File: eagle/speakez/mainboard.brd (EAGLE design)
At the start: 22 parts, among them U1 +12v

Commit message: disconnected battery from V3v3
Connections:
- net N$16: no longer U$1.7
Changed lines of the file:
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@@
 <contactref element="U$1" pad="30"/>
 <contactref element="U$1" pad="3"/>
-<contactref element="U$1" pad="7"/>
 <wire x1="-32.01" y1="-79.73" x2="-46.62" y2="-81.28" width="0" layer="19" extent="1-1"/>
 <wire x1="-17.5768" y1="-20.955" x2="-32.01" y2="-79.73" width="0" layer="19" extent="1-1"/>
 <wire x1="-14.605" y1="-11.4808" x2="-17.5768" y2="-20.955" width="0" layer="19" extent="1-1"/>
-<wire x1="-26.035" y1="-14.478" x2="-17.5768" y2="-20.955" width="0" layer="19" extent="1-1"/>
-<wire x1="-26.035" y1="-12.4968" x2="-26.035" y2="-14.478" width="0" layer="19" extent="1-1"/>
+<wire x1="-26.035" y1="-12.4968" x2="-14.605" y2="-11.4808" width="0" layer="19" extent="1-1"/>
 <wire x1="63.9064" y1="17.3228" x2="-14.605" y2="-11.4808" width="0" layer="19" extent="1-1"/>
 <wire x1="64.4" y1="24.13" x2="63.9064" y2="17.3228" width="0" layer="19" extent="1-1"/>

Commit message: changed clock pin
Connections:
- net TEST-PINS: no longer U$1.26
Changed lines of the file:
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@@
 <contactref element="VOICE" pad="1"/>
 <contactref element="TOAMBIENT" pad="2"/>
-<contactref element="U$1" pad="26"/>
 <wire x1="58.42" y1="35.37" x2="62.5" y2="46.99" width="0" layer="19" extent="1-1"/>
 <wire x1="64.6176" y1="18.2372" x2="58.42" y2="35.37" width="0" layer="19" extent="1-1"/>
-<wire x1="-19.558" y1="-20.955" x2="64.6176" y2="18.2372" width="0" layer="19" extent="1-1"/>
 </signal>
 <signal name="N$5">

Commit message: switched mic in to analog pins
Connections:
- net N$1: now also U$1.38
- net N$2: now also U$1.37
- net N$4: now also U$1.36; no longer U$1.11
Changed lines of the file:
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@@
 <contactref element="C1" pad="1"/>
 <contactref element="TESTPINS" pad="4"/>
+<contactref element="U$1" pad="38"/>
 <wire x1="58.42" y1="41.37" x2="62.55" y2="41.91" width="0" layer="19" extent="1-1"/>
 <wire x1="64.45" y1="36.83" x2="62.55" y2="41.91" width="0" layer="19" extent="1-1"/>
+<wire x1="-14.605" y1="-16.4846" x2="58.42" y2="41.37" width="0" layer="19" extent="1-1"/>
 </signal>
 <signal name="N$2">
@@
 <contactref element="C2" pad="1"/>
 <contactref element="TESTPINS" pad="5"/>
+<contactref element="U$1" pad="37"/>
 <wire x1="64.45" y1="31.75" x2="58.42" y2="43.37" width="0" layer="19" extent="1-1"/>
 <wire x1="62.55" y1="26.67" x2="64.45" y2="31.75" width="0" layer="19" extent="1-1"/>
+<wire x1="-14.605" y1="-16.9926" x2="62.55" y2="26.67" width="0" layer="19" extent="1-1"/>
 </signal>
 <signal name="GND">
@@
 <contactref element="R2" pad="1"/>
 <contactref element="TESTPINS" pad="3"/>
-<contactref element="U$1" pad="11"/>
+<contactref element="U$1" pad="36"/>
 <wire x1="62.55" y1="31.75" x2="58.42" y2="39.37" width="0" layer="19" extent="1-1"/>
 <wire x1="64.6176" y1="17.3228" x2="62.55" y2="31.75" width="0" layer="19" extent="1-1"/>
-<wire x1="-26.035" y1="-16.4846" x2="64.6176" y2="17.3228" width="0" layer="19" extent="1-1"/>
+<wire x1="-14.605" y1="-17.5006" x2="64.6176" y2="17.3228" width="0" layer="19" extent="1-1"/>
 </signal>
 <signal name="TEST-PINS">
@@
 <wire x1="64.4" y1="24.13" x2="63.9064" y2="17.3228" width="0" layer="19" extent="1-1"/>
 </signal>
+<signal name="N$18">
+</signal>
 </signals>

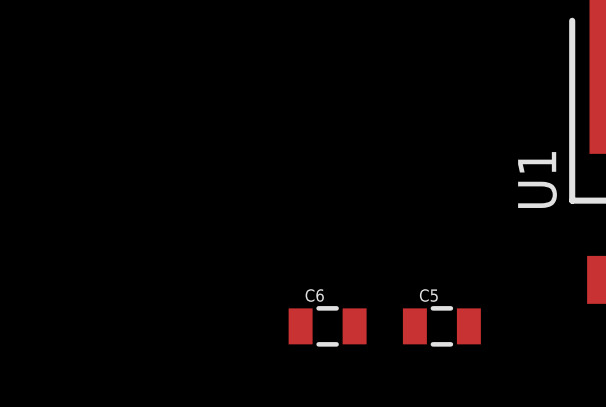
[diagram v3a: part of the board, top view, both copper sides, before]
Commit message: added 0.1uF caps
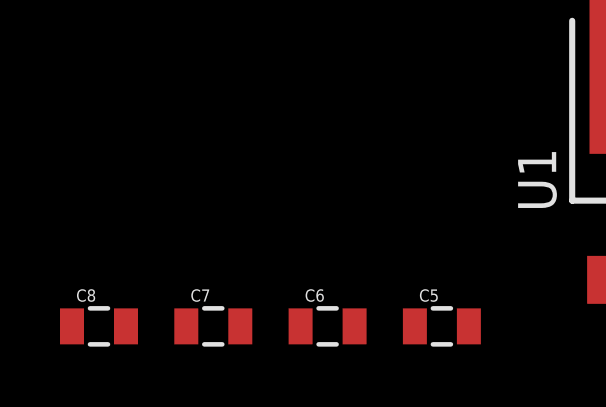
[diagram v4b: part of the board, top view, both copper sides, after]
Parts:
- added C7, C8: 0.1uF, SparkFun-Capacitors:0805
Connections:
- net N$14: now also C7.2, C8.2
- net N$15: now also C7.1
- net N$16: now also C8.1
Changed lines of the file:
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@@
 <element name="C5" library="SparkFun-Capacitors" package="0805" value="2.2uF" x="-41.91" y="-81.28"/>
 <element name="C6" library="SparkFun-Capacitors" package="0805" value="2.2uF" x="-45.72" y="-81.28"/>
+<element name="C7" library="SparkFun-Capacitors" package="0805" value="0.1uF" x="-49.53" y="-81.28"/>
+<element name="C8" library="SparkFun-Capacitors" package="0805" value="0.1uF" x="-53.34" y="-81.28"/>
 </elements>
 <signals>
@@
 <contactref element="U$1" pad="47"/>
 <contactref element="U$1" pad="4"/>
+<contactref element="C7" pad="2"/>
+<contactref element="C8" pad="2"/>
+<wire x1="-48.63" y1="-81.28" x2="-52.44" y2="-81.28" width="0" layer="19" extent="1-1"/>
+<wire x1="-44.82" y1="-81.28" x2="-48.63" y2="-81.28" width="0" layer="19" extent="1-1"/>
 <wire x1="-34.29" y1="-72.43" x2="-44.82" y2="-81.28" width="0" layer="19" extent="1-1"/>
 <wire x1="-17.0688" y1="-20.955" x2="-34.29" y2="-72.43" width="0" layer="19" extent="1-1"/>
@@
 <contactref element="D1" pad="C"/>
 <contactref element="C5" pad="1"/>
-<wire x1="-36.57" y1="-79.73" x2="84.125" y2="40.64" width="0" layer="19" extent="1-1"/>
-<wire x1="-42.81" y1="-81.28" x2="-36.57" y2="-79.73" width="0" layer="19" extent="1-1"/>
+<contactref element="C7" pad="1"/>
+<wire x1="-42.81" y1="-81.28" x2="-50.43" y2="-81.28" width="0" layer="19" extent="1-1"/>
+<wire x1="-36.57" y1="-79.73" x2="-42.81" y2="-81.28" width="0" layer="19" extent="1-1"/>
+<wire x1="84.125" y1="40.64" x2="-36.57" y2="-79.73" width="0" layer="19" extent="1-1"/>
 </signal>
 <signal name="N$16">
@@
 <contactref element="U$1" pad="30"/>
 <contactref element="U$1" pad="3"/>
+<contactref element="C8" pad="1"/>
+<wire x1="-46.62" y1="-81.28" x2="-54.24" y2="-81.28" width="0" layer="19" extent="1-1"/>
 <wire x1="-32.01" y1="-79.73" x2="-46.62" y2="-81.28" width="0" layer="19" extent="1-1"/>
 <wire x1="-17.5768" y1="-20.955" x2="-32.01" y2="-79.73" width="0" layer="19" extent="1-1"/>

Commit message: re-added the differential pins
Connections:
- net N$1: now also U$1.11
- net N$10: now also U$1.10
- net N$2: now also U$1.12
- net N$4: now also U$1.9
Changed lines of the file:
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@@
 <contactref element="TESTPINS" pad="4"/>
 <contactref element="U$1" pad="38"/>
+<contactref element="U$1" pad="11"/>
 <wire x1="58.42" y1="41.37" x2="62.55" y2="41.91" width="0" layer="19" extent="1-1"/>
 <wire x1="64.45" y1="36.83" x2="62.55" y2="41.91" width="0" layer="19" extent="1-1"/>
 <wire x1="-14.605" y1="-16.4846" x2="58.42" y2="41.37" width="0" layer="19" extent="1-1"/>
+<wire x1="-26.035" y1="-16.4846" x2="-14.605" y2="-16.4846" width="0" layer="19" extent="1-1"/>
 </signal>
 <signal name="N$2">
@@
 <contactref element="TESTPINS" pad="5"/>
 <contactref element="U$1" pad="37"/>
+<contactref element="U$1" pad="12"/>
 <wire x1="64.45" y1="31.75" x2="58.42" y2="43.37" width="0" layer="19" extent="1-1"/>
 <wire x1="62.55" y1="26.67" x2="64.45" y2="31.75" width="0" layer="19" extent="1-1"/>
 <wire x1="-14.605" y1="-16.9926" x2="62.55" y2="26.67" width="0" layer="19" extent="1-1"/>
+<wire x1="-26.035" y1="-16.9926" x2="-14.605" y2="-16.9926" width="0" layer="19" extent="1-1"/>
 </signal>
 <signal name="GND">
@@
 <contactref element="TESTPINS" pad="3"/>
 <contactref element="U$1" pad="36"/>
+<contactref element="U$1" pad="9"/>
 <wire x1="62.55" y1="31.75" x2="58.42" y2="39.37" width="0" layer="19" extent="1-1"/>
 <wire x1="64.6176" y1="17.3228" x2="62.55" y2="31.75" width="0" layer="19" extent="1-1"/>
 <wire x1="-14.605" y1="-17.5006" x2="64.6176" y2="17.3228" width="0" layer="19" extent="1-1"/>
+<wire x1="-26.035" y1="-15.494" x2="-14.605" y2="-17.5006" width="0" layer="19" extent="1-1"/>
 </signal>
 <signal name="TEST-PINS">
@@
 <contactref element="TESTPINS" pad="2"/>
 <contactref element="R1" pad="1"/>
+<contactref element="U$1" pad="10"/>
 <wire x1="62.55" y1="36.83" x2="66.5" y2="46.99" width="0" layer="19" extent="1-1"/>
 <wire x1="58.42" y1="37.37" x2="62.55" y2="36.83" width="0" layer="19" extent="1-1"/>
+<wire x1="-26.035" y1="-16.002" x2="58.42" y2="37.37" width="0" layer="19" extent="1-1"/>
 </signal>
 <signal name="N$9">

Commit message: connect VREFH and VBAT
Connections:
- new net N$3: U$1.14, U$1.21
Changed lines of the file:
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@@
 <signal name="N$18">
+</signal>
+<signal name="N$3">
+<contactref element="U$1" pad="14"/>
+<contactref element="U$1" pad="21"/>
+<wire x1="-22.0726" y1="-20.955" x2="-26.035" y2="-17.9832" width="0" layer="19" extent="1-1"/>
 </signal>
 </signals>

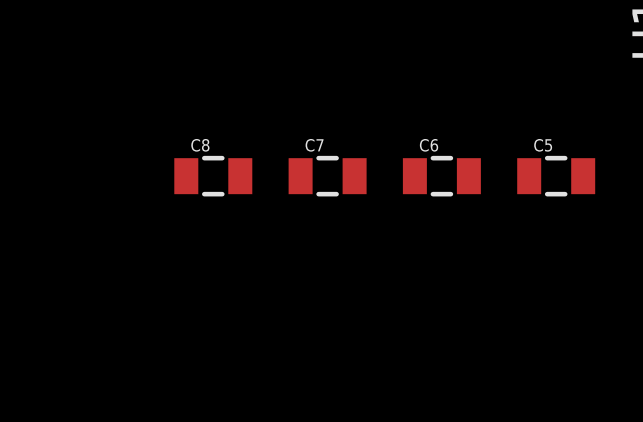
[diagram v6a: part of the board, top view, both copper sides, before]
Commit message: Added test LED
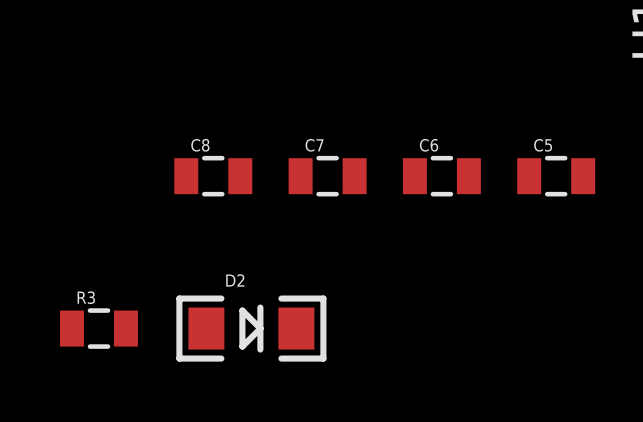
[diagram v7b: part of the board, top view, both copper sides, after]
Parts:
- added D2: (no value), SparkFun-LED:LED-1206
- added R3: 66 ohms, SparkFun-Passives:0805
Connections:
- new net N$17: D2.A, U$1.45
- new net N$19: D2.C, R3.2
- net GND: now also R3.1
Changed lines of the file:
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@@
 <element name="C7" library="SparkFun-Capacitors" package="0805" value="0.1uF" x="-49.53" y="-81.28"/>
 <element name="C8" library="SparkFun-Capacitors" package="0805" value="0.1uF" x="-53.34" y="-81.28"/>
+<element name="D2" library="SparkFun-LED" package="LED-1206" value="" x="-52.07" y="-86.36"/>
+<element name="R3" library="SparkFun-Passives" package="0805" value="66 ohms" x="-57.15" y="-86.36"/>
 </elements>
 <signals>
@@
 <contactref element="C4" pad="1"/>
 <contactref element="TOAMBIENT" pad="3"/>
-<wire x1="64.45" y1="41.91" x2="64.5" y2="46.99" width="0" layer="19" extent="1-1"/>
-<wire x1="64.45" y1="26.67" x2="64.45" y2="41.91" width="0" layer="19" extent="1-1"/>
-<wire x1="62.6" y1="24.13" x2="64.45" y2="26.67" width="0" layer="19" extent="1-1"/>
-<wire x1="63.9064" y1="18.2372" x2="62.6" y2="24.13" width="0" layer="19" extent="1-1"/>
-<wire x1="62.5348" y1="17.78" x2="63.9064" y2="18.2372" width="0" layer="19" extent="1-1"/>
-<wire x1="61.7728" y1="17.78" x2="62.5348" y2="17.78" width="0" layer="19" extent="1-1"/>
+<contactref element="R3" pad="1"/>
+<wire x1="61.7728" y1="17.78" x2="-58.05" y2="-86.36" width="0" layer="19" extent="1-1"/>
+<wire x1="62.5348" y1="17.78" x2="61.7728" y2="17.78" width="0" layer="19" extent="1-1"/>
+<wire x1="63.9064" y1="18.2372" x2="62.5348" y2="17.78" width="0" layer="19" extent="1-1"/>
+<wire x1="62.6" y1="24.13" x2="63.9064" y2="18.2372" width="0" layer="19" extent="1-1"/>
+<wire x1="64.45" y1="26.67" x2="62.6" y2="24.13" width="0" layer="19" extent="1-1"/>
+<wire x1="64.45" y1="41.91" x2="64.45" y2="26.67" width="0" layer="19" extent="1-1"/>
+<wire x1="64.5" y1="46.99" x2="64.45" y2="41.91" width="0" layer="19" extent="1-1"/>
 </signal>
 <signal name="N$4">
@@
 <wire x1="-22.0726" y1="-20.955" x2="-26.035" y2="-17.9832" width="0" layer="19" extent="1-1"/>
 </signal>
+<signal name="N$17">
+<contactref element="U$1" pad="45"/>
+<contactref element="D2" pad="A"/>
+<wire x1="-14.605" y1="-12.9794" x2="-53.57" y2="-86.36" width="0" layer="19" extent="1-1"/>
+</signal>
+<signal name="N$19">
+<contactref element="D2" pad="C"/>
+<contactref element="R3" pad="2"/>
+<wire x1="-50.57" y1="-86.36" x2="-56.25" y2="-86.36" width="0" layer="19" extent="1-1"/>
+</signal>
 </signals>

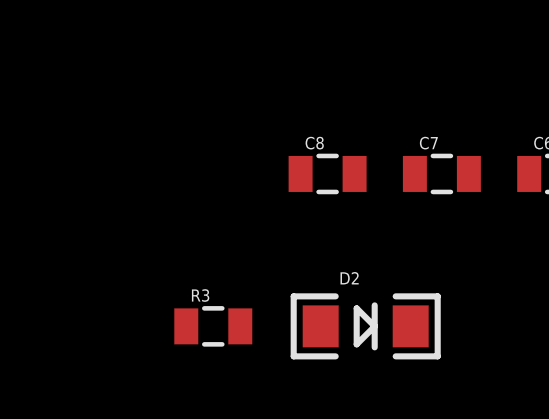
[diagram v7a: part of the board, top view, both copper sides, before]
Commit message: added pull-up resistor to RESET
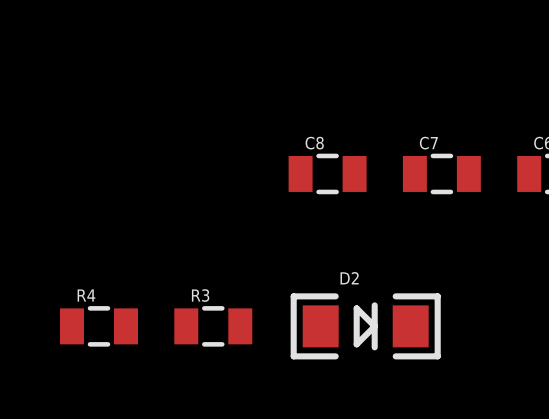
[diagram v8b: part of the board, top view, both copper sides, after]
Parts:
- added R4: 10k, SparkFun-Passives:0805
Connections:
- new net N$20: R4.1, U$1.34
- net GND: now also R4.2
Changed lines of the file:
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@@
 <element name="D2" library="SparkFun-LED" package="LED-1206" value="" x="-52.07" y="-86.36"/>
 <element name="R3" library="SparkFun-Passives" package="0805" value="66 ohms" x="-57.15" y="-86.36"/>
+<element name="R4" library="SparkFun-Passives" package="0805" value="10k" x="-60.96" y="-86.36"/>
 </elements>
 <signals>
@@
 <contactref element="TOAMBIENT" pad="3"/>
 <contactref element="R3" pad="1"/>
+<contactref element="R4" pad="2"/>
+<wire x1="-58.05" y1="-86.36" x2="-60.06" y2="-86.36" width="0" layer="19" extent="1-1"/>
 <wire x1="61.7728" y1="17.78" x2="-58.05" y2="-86.36" width="0" layer="19" extent="1-1"/>
 <wire x1="62.5348" y1="17.78" x2="61.7728" y2="17.78" width="0" layer="19" extent="1-1"/>
@@
 <wire x1="-50.57" y1="-86.36" x2="-56.25" y2="-86.36" width="0" layer="19" extent="1-1"/>
 </signal>
+<signal name="N$20">
+<contactref element="U$1" pad="34"/>
+<contactref element="R4" pad="1"/>
+<wire x1="-14.605" y1="-18.4912" x2="-61.86" y2="-86.36" width="0" layer="19" extent="1-1"/>
+</signal>
 </signals>
